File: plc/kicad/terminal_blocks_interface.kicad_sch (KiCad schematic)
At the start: 78 parts, among them CN1 DB128V-5.08-2P-GN-S, CN2 DB128V-5.08-2P-GN-S, CN3 DB128V-5.08-2P-GN-S, CN4 DB128V-5.08-2P-GN-S, CN5 DB128V-5.08-2P-GN-S, CN6 DB128V-5.08-2P-GN-S, CN7 DB128V-5.08-2P-GN-S, CN8 DB128V-5.08-2P-GN-S, CN9 DB128V-5.08-6P-GN-S, Q1 AO3400A, Q2 AO3400A, U1 TCA9535PWR, U2 TPS272C45DRHFR, U3 TPS272C45DRHFR, U4 ADS1115IDGSR, U5 LTV-814S-TA1-A, U6 LTV-814S-TA1-A, U7 LTV-814S-TA1-A, U8 LTV-814S-TA1-A

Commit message: AHT20 sensor added
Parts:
- C1, C10, C2, C3, C4, C5, C6, C7, C8, C9: footprint Capacitor_SMD:C_0805_2012Metric -> Capacitor_SMD:C_0603_1608Metric
- R1, R10, R11, R12, R13, R14, R15, R16, R17, R18, R19, R2, R20, R21, R22, R23, R24, R25, R26, R27, R28, R29, R3, R30, R31, R32, R33, R34, R35, R36, R37, R38, R39, R4, R40, R41, R42, R43, R5, R6, R7, R8, R9: footprint Resistor_SMD:R_0805_2012Metric -> Resistor_SMD:R_0603_1608Metric
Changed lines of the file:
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@@
 			)
 		)
-		(property "Footprint" "Resistor_SMD:R_0805_2012Metric"
+		(property "Footprint" "Resistor_SMD:R_0603_1608Metric"
 			(at 21.336 138.557 90)
 			(hide yes)
@@
 			)
 		)
-		(property "Footprint" "Resistor_SMD:R_0805_2012Metric"
+		(property "Footprint" "Resistor_SMD:R_0603_1608Metric"
 			(at 48.768 237.871 90)
 			(hide yes)
@@
 			)
 		)
-		(property "Footprint" "Resistor_SMD:R_0805_2012Metric"
+		(property "Footprint" "Resistor_SMD:R_0603_1608Metric"
 			(at 173.99 91.567 90)
 			(hide yes)
@@
 			)
 		)
-		(property "Footprint" "Capacitor_SMD:C_0805_2012Metric"
+		(property "Footprint" "Capacitor_SMD:C_0603_1608Metric"
 			(at 228.4222 75.057 0)
 			(hide yes)
@@
 			)
 		)
-		(property "Footprint" "Resistor_SMD:R_0805_2012Metric"
+		(property "Footprint" "Resistor_SMD:R_0603_1608Metric"
 			(at 221.742 35.179 90)
 			(hide yes)
@@
 			)
 		)
-		(property "Footprint" "Resistor_SMD:R_0805_2012Metric"
+		(property "Footprint" "Resistor_SMD:R_0603_1608Metric"
 			(at 177.292 41.91 90)
 			(hide yes)
@@
 			)
 		)
-		(property "Footprint" "Resistor_SMD:R_0805_2012Metric"
+		(property "Footprint" "Resistor_SMD:R_0603_1608Metric"
 			(at 294.005 36.068 90)
 			(hide yes)
@@
 			)
 		)
-		(property "Footprint" "Resistor_SMD:R_0805_2012Metric"
+		(property "Footprint" "Resistor_SMD:R_0603_1608Metric"
 			(at 22.733 197.104 90)
 			(hide yes)
@@
 			)
 		)
-		(property "Footprint" "Resistor_SMD:R_0805_2012Metric"
+		(property "Footprint" "Resistor_SMD:R_0603_1608Metric"
 			(at 173.99 63.627 90)
 			(hide yes)
@@
 			)
 		)
-		(property "Footprint" "Capacitor_SMD:C_0805_2012Metric"
+		(property "Footprint" "Capacitor_SMD:C_0603_1608Metric"
 			(at 43.7642 169.037 0)
 			(hide yes)
@@
 			)
 		)
-		(property "Footprint" "Resistor_SMD:R_0805_2012Metric"
+		(property "Footprint" "Resistor_SMD:R_0603_1608Metric"
 			(at 301.498 40.005 90)
 			(hide yes)
@@
 			)
 		)
-		(property "Footprint" "Resistor_SMD:R_0805_2012Metric"
+		(property "Footprint" "Resistor_SMD:R_0603_1608Metric"
 			(at 35.433 236.474 90)
 			(hide yes)
@@
 			)
 		)
-		(property "Footprint" "Resistor_SMD:R_0805_2012Metric"
+		(property "Footprint" "Resistor_SMD:R_0603_1608Metric"
 			(at 35.306 121.412 90)
 			(hide yes)
@@
 			)
 		)
-		(property "Footprint" "Resistor_SMD:R_0805_2012Metric"
+		(property "Footprint" "Resistor_SMD:R_0603_1608Metric"
 			(at 217.805 42.037 90)
 			(hide yes)
@@
 			)
 		)
-		(property "Footprint" "Capacitor_SMD:C_0805_2012Metric"
+		(property "Footprint" "Capacitor_SMD:C_0603_1608Metric"
 			(at 60.2742 169.164 0)
 			(hide yes)
@@
 			)
 		)
-		(property "Footprint" "Resistor_SMD:R_0805_2012Metric"
+		(property "Footprint" "Resistor_SMD:R_0603_1608Metric"
 			(at 22.606 99.187 90)
 			(hide yes)
@@
 			)
 		)
-		(property "Footprint" "Resistor_SMD:R_0805_2012Metric"
+		(property "Footprint" "Resistor_SMD:R_0603_1608Metric"
 			(at 221.742 92.329 90)
 			(hide yes)
@@
 			)
 		)
-		(property "Footprint" "Resistor_SMD:R_0805_2012Metric"
+		(property "Footprint" "Resistor_SMD:R_0603_1608Metric"
 			(at 173.99 34.417 90)
 			(hide yes)
@@
 			)
 		)
-		(property "Footprint" "Resistor_SMD:R_0805_2012Metric"
+		(property "Footprint" "Resistor_SMD:R_0603_1608Metric"
 			(at 22.098 216.789 90)
 			(hide yes)
@@
 			)
 		)
-		(property "Footprint" "Capacitor_SMD:C_0805_2012Metric"
+		(property "Footprint" "Capacitor_SMD:C_0603_1608Metric"
 			(at 228.4222 45.847 0)
 			(hide yes)
@@
 			)
 		)
-		(property "Footprint" "Resistor_SMD:R_0805_2012Metric"
+		(property "Footprint" "Resistor_SMD:R_0603_1608Metric"
 			(at 35.306 99.06 90)
 			(hide yes)
@@
 			)
 		)
-		(property "Footprint" "Resistor_SMD:R_0805_2012Metric"
+		(property "Footprint" "Resistor_SMD:R_0603_1608Metric"
 			(at 217.805 99.187 90)
 			(hide yes)
@@
 			)
 		)
-		(property "Footprint" "Resistor_SMD:R_0805_2012Metric"
+		(property "Footprint" "Resistor_SMD:R_0603_1608Metric"
 			(at 173.99 121.412 90)
 			(hide yes)
@@
 			)
 		)
-		(property "Footprint" "Resistor_SMD:R_0805_2012Metric"
+		(property "Footprint" "Resistor_SMD:R_0603_1608Metric"
 			(at 25.908 263.144 90)
 			(hide yes)
@@
 			)
 		)
-		(property "Footprint" "Resistor_SMD:R_0805_2012Metric"
+		(property "Footprint" "Resistor_SMD:R_0603_1608Metric"
 			(at 217.805 129.032 90)
 			(hide yes)
@@
 			)
 		)
-		(property "Footprint" "Capacitor_SMD:C_0805_2012Metric"
+		(property "Footprint" "Capacitor_SMD:C_0603_1608Metric"
 			(at 228.4222 132.842 0)
 			(hide yes)
@@
 			)
 		)
-		(property "Footprint" "Resistor_SMD:R_0805_2012Metric"
+		(property "Footprint" "Resistor_SMD:R_0603_1608Metric"
 			(at 48.641 197.231 90)
 			(hide yes)
@@
 			)
 		)
-		(property "Footprint" "Resistor_SMD:R_0805_2012Metric"
+		(property "Footprint" "Resistor_SMD:R_0603_1608Metric"
 			(at 35.179 161.29 90)
 			(hide yes)
@@
 			)
 		)
-		(property "Footprint" "Resistor_SMD:R_0805_2012Metric"
+		(property "Footprint" "Resistor_SMD:R_0603_1608Metric"
 			(at 177.292 128.905 90)
 			(hide yes)
@@
 			)
 		)
-		(property "Footprint" "Resistor_SMD:R_0805_2012Metric"
+		(property "Footprint" "Resistor_SMD:R_0603_1608Metric"
 			(at 35.306 259.207 90)
 			(hide yes)
@@
 			)
 		)
-		(property "Footprint" "Resistor_SMD:R_0805_2012Metric"
+		(property "Footprint" "Resistor_SMD:R_0603_1608Metric"
 			(at 35.433 196.977 90)
 			(hide yes)
@@
 			)
 		)
-		(property "Footprint" "Resistor_SMD:R_0805_2012Metric"
+		(property "Footprint" "Resistor_SMD:R_0603_1608Metric"
 			(at 21.971 118.872 90)
 			(hide yes)
@@
 			)
 		)
-		(property "Footprint" "Resistor_SMD:R_0805_2012Metric"
+		(property "Footprint" "Resistor_SMD:R_0603_1608Metric"
 			(at 48.641 139.954 90)
 			(hide yes)
@@
 			)
 		)
-		(property "Footprint" "Capacitor_SMD:C_0805_2012Metric"
+		(property "Footprint" "Capacitor_SMD:C_0603_1608Metric"
 			(at 73.4822 169.164 0)
 			(hide yes)
@@
 			)
 		)
-		(property "Footprint" "Resistor_SMD:R_0805_2012Metric"
+		(property "Footprint" "Resistor_SMD:R_0603_1608Metric"
 			(at 48.514 99.314 90)
 			(hide yes)
@@
 			)
 		)
-		(property "Footprint" "Resistor_SMD:R_0805_2012Metric"
+		(property "Footprint" "Resistor_SMD:R_0603_1608Metric"
 			(at 48.641 121.412 90)
 			(hide yes)
@@
 			)
 		)
-		(property "Footprint" "Capacitor_SMD:C_0805_2012Metric"
+		(property "Footprint" "Capacitor_SMD:C_0603_1608Metric"
 			(at 228.4222 102.997 0)
 			(hide yes)
@@
 			)
 		)
-		(property "Footprint" "Resistor_SMD:R_0805_2012Metric"
+		(property "Footprint" "Resistor_SMD:R_0603_1608Metric"
 			(at 99.187 47.625 90)
 			(hide yes)
@@
 			)
 		)
-		(property "Footprint" "Resistor_SMD:R_0805_2012Metric"
+		(property "Footprint" "Resistor_SMD:R_0603_1608Metric"
 			(at 35.433 219.329 90)
 			(hide yes)
@@
 			)
 		)
-		(property "Footprint" "Resistor_SMD:R_0805_2012Metric"
+		(property "Footprint" "Resistor_SMD:R_0603_1608Metric"
 			(at 177.292 71.12 90)
 			(hide yes)
@@
 			)
 		)
-		(property "Footprint" "Resistor_SMD:R_0805_2012Metric"
+		(property "Footprint" "Resistor_SMD:R_0603_1608Metric"
 			(at 21.463 236.474 90)
 			(hide yes)
@@
 			)
 		)
-		(property "Footprint" "Capacitor_SMD:C_0805_2012Metric"
+		(property "Footprint" "Capacitor_SMD:C_0603_1608Metric"
 			(at 60.4012 267.081 0)
 			(hide yes)
@@
 			)
 		)
-		(property "Footprint" "Resistor_SMD:R_0805_2012Metric"
+		(property "Footprint" "Resistor_SMD:R_0603_1608Metric"
 			(at 221.742 122.174 90)
 			(hide yes)
@@
 			)
 		)
-		(property "Footprint" "Resistor_SMD:R_0805_2012Metric"
+		(property "Footprint" "Resistor_SMD:R_0603_1608Metric"
 			(at 294.005 64.008 90)
 			(hide yes)
@@
 			)
 		)
-		(property "Footprint" "Resistor_SMD:R_0805_2012Metric"
+		(property "Footprint" "Resistor_SMD:R_0603_1608Metric"
 			(at 35.306 138.557 90)
 			(hide yes)
@@
 			)
 		)
-		(property "Footprint" "Capacitor_SMD:C_0805_2012Metric"
+		(property "Footprint" "Capacitor_SMD:C_0603_1608Metric"
 			(at 43.8912 266.954 0)
 			(hide yes)
@@
 			)
 		)
-		(property "Footprint" "Resistor_SMD:R_0805_2012Metric"
+		(property "Footprint" "Resistor_SMD:R_0603_1608Metric"
 			(at 301.498 67.945 90)
 			(hide yes)
@@
 			)
 		)
-		(property "Footprint" "Resistor_SMD:R_0805_2012Metric"
+		(property "Footprint" "Resistor_SMD:R_0603_1608Metric"
 			(at 48.768 219.329 90)
 			(hide yes)
@@
 			)
 		)
-		(property "Footprint" "Resistor_SMD:R_0805_2012Metric"
+		(property "Footprint" "Resistor_SMD:R_0603_1608Metric"
 			(at 221.742 64.389 90)
 			(hide yes)
@@
 			)
 		)
-		(property "Footprint" "Capacitor_SMD:C_0805_2012Metric"
+		(property "Footprint" "Capacitor_SMD:C_0603_1608Metric"
 			(at 73.6092 267.081 0)
 			(hide yes)
@@
 			)
 		)
-		(property "Footprint" "Resistor_SMD:R_0805_2012Metric"
+		(property "Footprint" "Resistor_SMD:R_0603_1608Metric"
 			(at 25.781 165.227 90)
 			(hide yes)
@@
 			)
 		)
-		(property "Footprint" "Resistor_SMD:R_0805_2012Metric"
+		(property "Footprint" "Resistor_SMD:R_0603_1608Metric"
 			(at 217.805 71.247 90)
 			(hide yes)
@@
 			)
 		)
-		(property "Footprint" "Resistor_SMD:R_0805_2012Metric"
+		(property "Footprint" "Resistor_SMD:R_0603_1608Metric"
 			(at 177.292 99.06 90)
 			(hide yes)

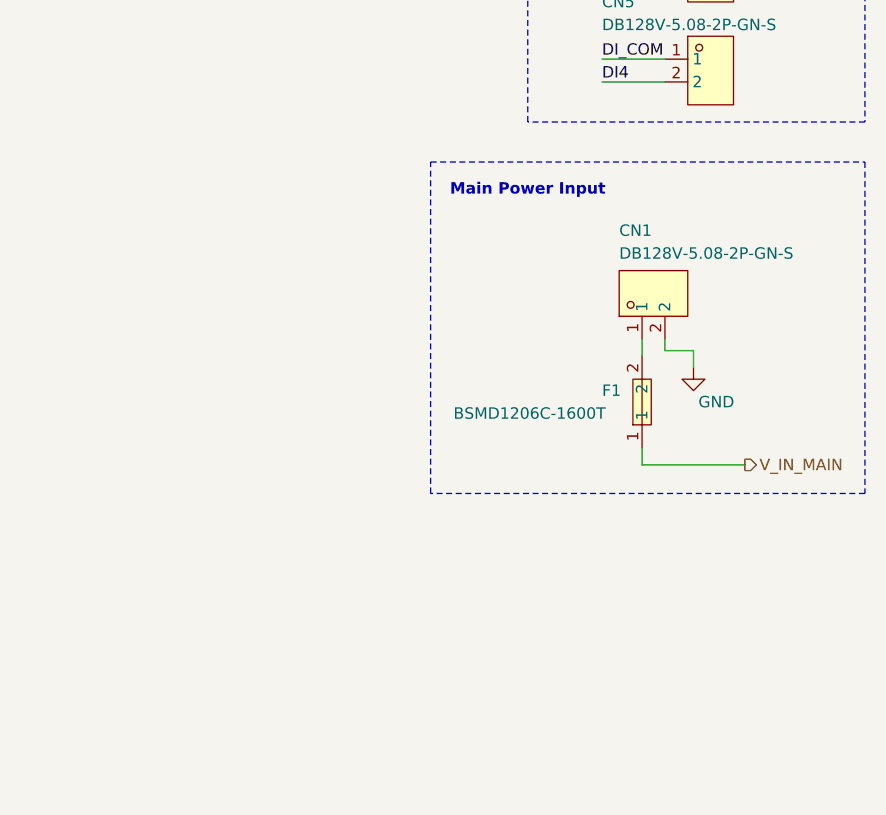
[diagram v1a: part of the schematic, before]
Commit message: Added another power connector
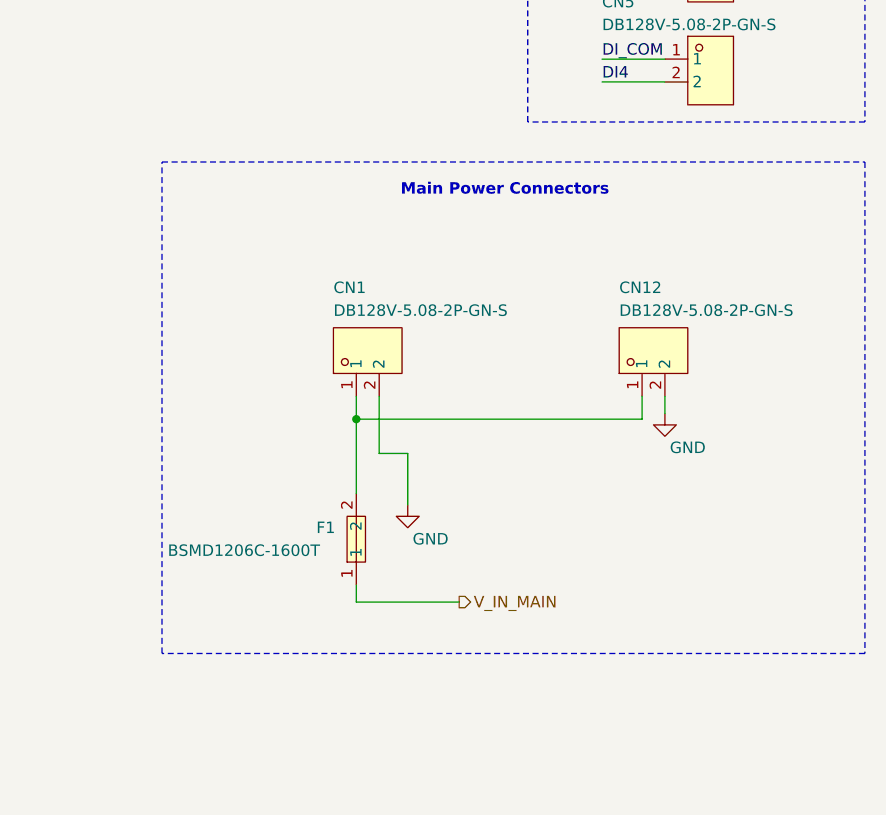
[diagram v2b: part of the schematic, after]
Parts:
- added CN12: DB128V-5.08-2P-GN-S, LibrePLC32:CONN-TH_2P-P5.08_DIBO_DB128V-5.08, symbol LibrePLC32:DB128V-5.08-2P-GN-S
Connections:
- net GND: now also CN12.2
- net at CN1.1, F1.2: now also CN12.1
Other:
- note added: "Main Power Connectors"
- note removed: "Main Power Input"
- moved on the sheet: CN1, F1

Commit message: PCB placement
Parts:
- renumbered CN9 to CN10, CN12 to CN2, CN6 to CN3, CN7 to CN4, CN8 to CN5, CN2 to CN6, CN3 to CN7, CN4 to CN8, CN5 to CN9
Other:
- title: (none) -> LibrePLC32
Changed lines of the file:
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@@
 	(generator_version "10.0")
 	(paper "A3")
+	(title_block
+		(title "LibrePLC32")
+		(date "2026-04-12")
+		(rev "A")
+	)
 	(rectangle
 		(start 127 247.015)
@@
 		(in_pos_files yes)
 		(dnp no)
-		(property "Reference" "#PWR0234"
+		(property "Reference" "#PWR068"
 			(at 377.19 213.36 0)
 			(hide yes)
@@
 			(project "LibrePLC32"
 				(path "/ef4c1a27-85a3-413a-9f93-a41c4f97eee5/7299de7e-bdc9-4cc1-ab0f-f2b9af304cf6"
-					(reference "#PWR0234")
+					(reference "#PWR068")
 					(unit 1)
 				)
@@
 		(in_pos_files yes)
 		(dnp no)
-		(property "Reference" "CN4"
+		(property "Reference" "CN8"
 			(at 370.205 149.86 0)
 			(show_name no)
@@
 			(project "LibrePLC32"
 				(path "/ef4c1a27-85a3-413a-9f93-a41c4f97eee5/7299de7e-bdc9-4cc1-ab0f-f2b9af304cf6"
-					(reference "CN4")
+					(reference "CN8")
 					(unit 1)
 				)
@@
 		(in_pos_files yes)
 		(dnp no)
-		(property "Reference" "CN9"
+		(property "Reference" "CN10"
 			(at 370.205 90.805 0)
 			(show_name no)
@@
 			(project "LibrePLC32"
 				(path "/ef4c1a27-85a3-413a-9f93-a41c4f97eee5/7299de7e-bdc9-4cc1-ab0f-f2b9af304cf6"
-					(reference "CN9")
+					(reference "CN10")
 					(unit 1)
 				)
@@
 		(in_pos_files yes)
 		(dnp no)
-		(property "Reference" "CN8"
+		(property "Reference" "CN5"
 			(at 368.3 59.055 0)
 			(show_name no)
@@
 			(project "LibrePLC32"
 				(path "/ef4c1a27-85a3-413a-9f93-a41c4f97eee5/7299de7e-bdc9-4cc1-ab0f-f2b9af304cf6"
-					(reference "CN8")
+					(reference "CN5")
 					(unit 1)
 				)
@@
 		(dnp no)
 		(fields_autoplaced yes)
-		(property "Reference" "#PWR066"
+		(property "Reference" "#PWR067"
 			(at 370.84 100.33 0)
 			(hide yes)
@@
 			(project "LibrePLC32"
 				(path "/ef4c1a27-85a3-413a-9f93-a41c4f97eee5/7299de7e-bdc9-4cc1-ab0f-f2b9af304cf6"
-					(reference "#PWR066")
+					(reference "#PWR067")
 					(unit 1)
 				)
@@
 		(dnp no)
 		(fields_autoplaced yes)
-		(property "Reference" "#PWR065"
+		(property "Reference" "#PWR066"
 			(at 381 97.79 0)
 			(hide yes)
@@
 			(project "LibrePLC32"
 				(path "/ef4c1a27-85a3-413a-9f93-a41c4f97eee5/7299de7e-bdc9-4cc1-ab0f-f2b9af304cf6"
-					(reference "#PWR065")
+					(reference "#PWR066")
 					(unit 1)
 				)
@@
 		(in_pos_files yes)
 		(dnp no)
-		(property "Reference" "CN5"
+		(property "Reference" "CN9"
 			(at 370.205 161.29 0)
 			(show_name no)
@@
 			(project "LibrePLC32"
 				(path "/ef4c1a27-85a3-413a-9f93-a41c4f97eee5/7299de7e-bdc9-4cc1-ab0f-f2b9af304cf6"
-					(reference "CN5")
+					(reference "CN9")
 					(unit 1)
 				)
@@
 		(in_pos_files yes)
 		(dnp no)
-		(property "Reference" "#PWR067"
+		(property "Reference" "#PWR065"
 			(at 348.615 223.52 0)
 			(hide yes)
@@
 			(project "LibrePLC32"
 				(path "/ef4c1a27-85a3-413a-9f93-a41c4f97eee5/7299de7e-bdc9-4cc1-ab0f-f2b9af304cf6"
-					(reference "#PWR067")
+					(reference "#PWR065")
 					(unit 1)
 				)
@@
 		(in_pos_files yes)
 		(dnp no)
-		(property "Reference" "CN12"
+		(property "Reference" "CN2"
 			(at 372.11 193.04 90)
 			(show_name no)
@@
 			(project "LibrePLC32"
 				(path "/ef4c1a27-85a3-413a-9f93-a41c4f97eee5/7299de7e-bdc9-4cc1-ab0f-f2b9af304cf6"
-					(reference "CN12")
+					(reference "CN2")
 					(unit 1)
 				)
@@
 		(in_pos_files yes)
 		(dnp no)
-		(property "Reference" "CN2"
+		(property "Reference" "CN6"
 			(at 370.205 125.73 0)
 			(show_name no)
@@
 			(project "LibrePLC32"
 				(path "/ef4c1a27-85a3-413a-9f93-a41c4f97eee5/7299de7e-bdc9-4cc1-ab0f-f2b9af304cf6"
-					(reference "CN2")
+					(reference "CN6")
 					(unit 1)
 				)
@@
 		(in_pos_files yes)
 		(dnp no)
-		(property "Reference" "CN3"
+		(property "Reference" "CN7"
 			(at 370.205 137.795 0)
 			(show_name no)
@@
 			(project "LibrePLC32"
 				(path "/ef4c1a27-85a3-413a-9f93-a41c4f97eee5/7299de7e-bdc9-4cc1-ab0f-f2b9af304cf6"
-					(reference "CN3")
+					(reference "CN7")
 					(unit 1)
 				)
@@
 		(in_pos_files yes)
 		(dnp no)
-		(property "Reference" "CN7"
+		(property "Reference" "CN4"
 			(at 368.3 43.18 0)
 			(show_name no)
@@
 			(project "LibrePLC32"
 				(path "/ef4c1a27-85a3-413a-9f93-a41c4f97eee5/7299de7e-bdc9-4cc1-ab0f-f2b9af304cf6"
-					(reference "CN7")
+					(reference "CN4")
 					(unit 1)
 				)
@@
 		(in_pos_files yes)
 		(dnp no)
-		(property "Reference" "CN6"
+		(property "Reference" "CN3"
 			(at 368.3 28.575 0)
 			(show_name no)
@@
 			(project "LibrePLC32"
 				(path "/ef4c1a27-85a3-413a-9f93-a41c4f97eee5/7299de7e-bdc9-4cc1-ab0f-f2b9af304cf6"
-					(reference "CN6")
+					(reference "CN3")
 					(unit 1)
 				)
